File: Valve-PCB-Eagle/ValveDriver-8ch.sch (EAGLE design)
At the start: 17 parts, among them IC1 ULQ2803A, J10 Valve 3, J11 Valve 2, J12 Valve 1, J4 POWER_JACK, J5 Valve 8, J6 Valve 7, J7 Valve 6, J8 Valve 5, J9 Valve 4

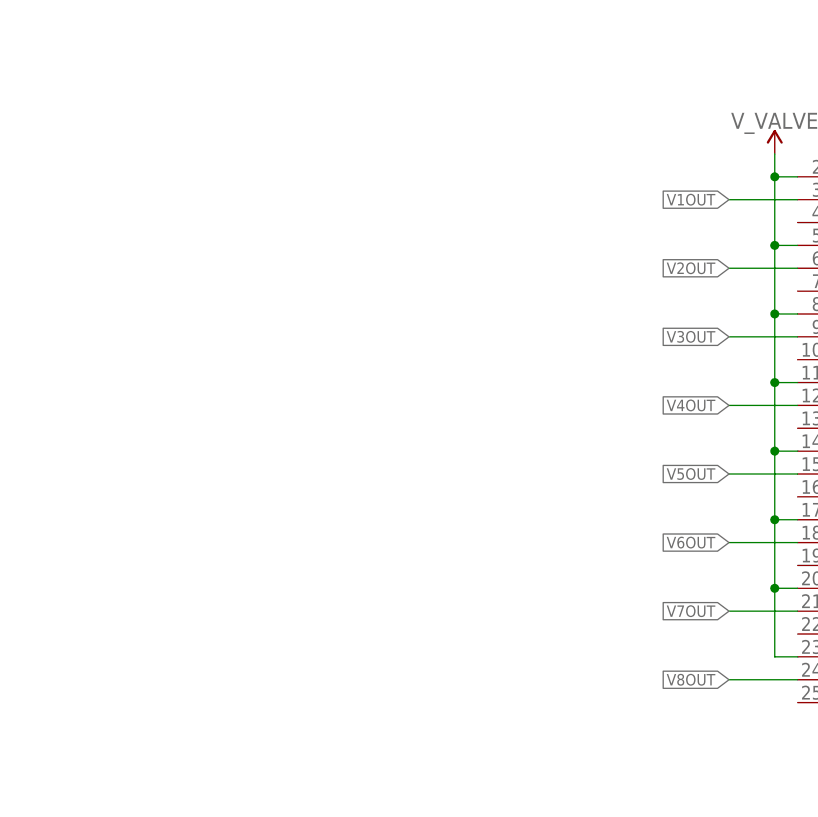
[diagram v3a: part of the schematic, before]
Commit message: [Valve] Add momentary push buttons (fixes #1)
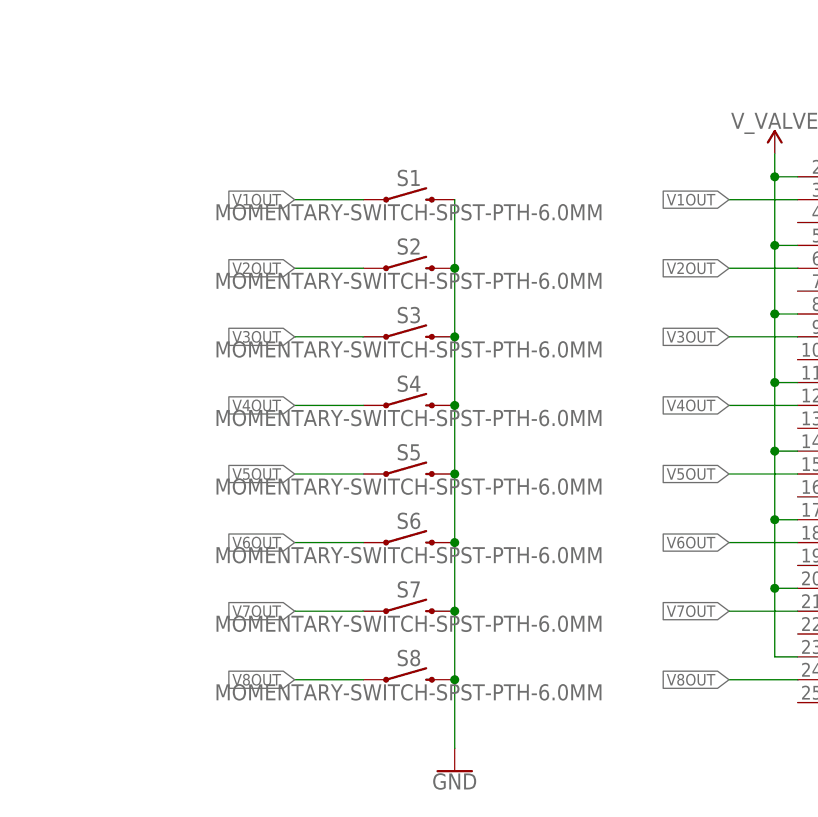
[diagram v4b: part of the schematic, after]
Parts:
- added S1, S2, S3, S4, S5, S6, S7, S8: MOMENTARY-SWITCH-SPST-PTH-6.0MM, SparkFun-Switches:MOMENTARY-SWITCH-SPST-PTH-6.0MM
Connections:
- net GND: now also S1.2, S2.2, S3.2, S4.2, S5.2, S6.2, S7.2, S8.2
- net V1OUT: now also S1.1
- net V2OUT: now also S2.1
- net V3OUT: now also S3.1
- net V4OUT: now also S4.1
- net V5OUT: now also S5.1
- net V6OUT: now also S6.1
- net V7OUT: now also S7.1
- net V8OUT: now also S8.1
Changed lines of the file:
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@@
 <part name="J2" library="SparkFun-Connectors" library_urn="urn:adsk.eagle:library:513" deviceset="CONN_24" device="" package3d_urn="urn:adsk.eagle:package:38202/1"/>
 <part name="SUPPLY13" library="SparkFun-PowerSymbols" library_urn="urn:adsk.eagle:library:530" deviceset="VCC_1" device="" value="V_VALVE"/>
+<part name="S1" library="SparkFun-Switches" library_urn="urn:adsk.eagle:library:535" deviceset="MOMENTARY-SWITCH-SPST" device="-PTH-6.0MM" package3d_urn="urn:adsk.eagle:package:40163/1"/>
+<part name="S2" library="SparkFun-Switches" library_urn="urn:adsk.eagle:library:535" deviceset="MOMENTARY-SWITCH-SPST" device="-PTH-6.0MM" package3d_urn="urn:adsk.eagle:package:40163/1"/>
+<part name="S3" library="SparkFun-Switches" library_urn="urn:adsk.eagle:library:535" deviceset="MOMENTARY-SWITCH-SPST" device="-PTH-6.0MM" package3d_urn="urn:adsk.eagle:package:40163/1"/>
+<part name="S4" library="SparkFun-Switches" library_urn="urn:adsk.eagle:library:535" deviceset="MOMENTARY-SWITCH-SPST" device="-PTH-6.0MM" package3d_urn="urn:adsk.eagle:package:40163/1"/>
+<part name="S5" library="SparkFun-Switches" library_urn="urn:adsk.eagle:library:535" deviceset="MOMENTARY-SWITCH-SPST" device="-PTH-6.0MM" package3d_urn="urn:adsk.eagle:package:40163/1"/>
+<part name="S6" library="SparkFun-Switches" library_urn="urn:adsk.eagle:library:535" deviceset="MOMENTARY-SWITCH-SPST" device="-PTH-6.0MM" package3d_urn="urn:adsk.eagle:package:40163/1"/>
+<part name="S7" library="SparkFun-Switches" library_urn="urn:adsk.eagle:library:535" deviceset="MOMENTARY-SWITCH-SPST" device="-PTH-6.0MM" package3d_urn="urn:adsk.eagle:package:40163/1"/>
+<part name="S8" library="SparkFun-Switches" library_urn="urn:adsk.eagle:library:535" deviceset="MOMENTARY-SWITCH-SPST" device="-PTH-6.0MM" package3d_urn="urn:adsk.eagle:package:40163/1"/>
+<part name="GND1" library="SparkFun-PowerSymbols" deviceset="GND" device=""/>
 </parts>
 <sheets>
@@
 <attribute name="VALUE" x="76.2" y="7.874" size="1.778" layer="96" align="bottom-center"/>
 </instance>
+<instance part="S1" gate="G$1" x="35.56" y="0" smashed="yes">
+<attribute name="NAME" x="35.56" y="1.524" size="1.778" layer="95" font="vector" align="bottom-center"/>
+<attribute name="VALUE" x="35.56" y="-0.508" size="1.778" layer="96" font="vector" align="top-center"/>
+</instance>
+<instance part="S2" gate="G$1" x="35.56" y="-7.62" smashed="yes">
+<attribute name="NAME" x="35.56" y="-6.096" size="1.778" layer="95" font="vector" align="bottom-center"/>
+<attribute name="VALUE" x="35.56" y="-8.128" size="1.778" layer="96" font="vector" align="top-center"/>
+</instance>
+<instance part="S3" gate="G$1" x="35.56" y="-15.24" smashed="yes">
+<attribute name="NAME" x="35.56" y="-13.716" size="1.778" layer="95" font="vector" align="bottom-center"/>
+<attribute name="VALUE" x="35.56" y="-15.748" size="1.778" layer="96" font="vector" align="top-center"/>
+</instance>
+<instance part="S4" gate="G$1" x="35.56" y="-22.86" smashed="yes">
+<attribute name="NAME" x="35.56" y="-21.336" size="1.778" layer="95" font="vector" align="bottom-center"/>
+<attribute name="VALUE" x="35.56" y="-23.368" size="1.778" layer="96" font="vector" align="top-center"/>
+</instance>
+<instance part="S5" gate="G$1" x="35.56" y="-30.48" smashed="yes">
+<attribute name="NAME" x="35.56" y="-28.956" size="1.778" layer="95" font="vector" align="bottom-center"/>
+<attribute name="VALUE" x="35.56" y="-30.988" size="1.778" layer="96" font="vector" align="top-center"/>
+</instance>
+<instance part="S6" gate="G$1" x="35.56" y="-38.1" smashed="yes">
+<attribute name="NAME" x="35.56" y="-36.576" size="1.778" layer="95" font="vector" align="bottom-center"/>
+<attribute name="VALUE" x="35.56" y="-38.608" size="1.778" layer="96" font="vector" align="top-center"/>
+</instance>
+<instance part="S7" gate="G$1" x="35.56" y="-45.72" smashed="yes">
+<attribute name="NAME" x="35.56" y="-44.196" size="1.778" layer="95" font="vector" align="bottom-center"/>
+<attribute name="VALUE" x="35.56" y="-46.228" size="1.778" layer="96" font="vector" align="top-center"/>
+</instance>
+<instance part="S8" gate="G$1" x="35.56" y="-53.34" smashed="yes">
+<attribute name="NAME" x="35.56" y="-51.816" size="1.778" layer="95" font="vector" align="bottom-center"/>
+<attribute name="VALUE" x="35.56" y="-53.848" size="1.778" layer="96" font="vector" align="top-center"/>
+</instance>
+<instance part="GND1" gate="1" x="40.64" y="-63.5" smashed="yes">
+<attribute name="VALUE" x="40.64" y="-63.754" size="1.778" layer="96" align="top-center"/>
+</instance>
 </instances>
 <busses>
@@
 <pinref part="J14" gate="G$1" pin="1"/>
 <pinref part="GND11" gate="1" pin="GND"/>
+</segment>
+<segment>
+<pinref part="GND1" gate="1" pin="GND"/>
+<pinref part="S8" gate="G$1" pin="2"/>
+<wire x1="40.64" y1="-60.96" x2="40.64" y2="-53.34" width="0.1524" layer="91"/>
+<pinref part="S7" gate="G$1" pin="2"/>
+<wire x1="40.64" y1="-53.34" x2="40.64" y2="-45.72" width="0.1524" layer="91"/>
+<junction x="40.64" y="-53.34"/>
+<pinref part="S6" gate="G$1" pin="2"/>
+<wire x1="40.64" y1="-45.72" x2="40.64" y2="-38.1" width="0.1524" layer="91"/>
+<junction x="40.64" y="-45.72"/>
+<pinref part="S5" gate="G$1" pin="2"/>
+<wire x1="40.64" y1="-38.1" x2="40.64" y2="-30.48" width="0.1524" layer="91"/>
+<junction x="40.64" y="-38.1"/>
+<pinref part="S4" gate="G$1" pin="2"/>
+<wire x1="40.64" y1="-30.48" x2="40.64" y2="-22.86" width="0.1524" layer="91"/>
+<junction x="40.64" y="-30.48"/>
+<pinref part="S3" gate="G$1" pin="2"/>
+<wire x1="40.64" y1="-22.86" x2="40.64" y2="-15.24" width="0.1524" layer="91"/>
+<junction x="40.64" y="-22.86"/>
+<pinref part="S2" gate="G$1" pin="2"/>
+<wire x1="40.64" y1="-15.24" x2="40.64" y2="-7.62" width="0.1524" layer="91"/>
+<junction x="40.64" y="-15.24"/>
+<pinref part="S1" gate="G$1" pin="2"/>
+<wire x1="40.64" y1="-7.62" x2="40.64" y2="0" width="0.1524" layer="91"/>
+<junction x="40.64" y="-7.62"/>
 </segment>
 </net>
@@
 <label x="71.12" y="-53.34" size="1.27" layer="95" rot="R180" xref="yes"/>
 </segment>
+<segment>
+<wire x1="30.48" y1="-53.34" x2="22.86" y2="-53.34" width="0.1524" layer="91"/>
+<label x="22.86" y="-53.34" size="1.27" layer="95" rot="R180" xref="yes"/>
+<pinref part="S8" gate="G$1" pin="1"/>
+</segment>
 </net>
 <net name="V7OUT" class="1">
@@
 <label x="71.12" y="-45.72" size="1.27" layer="95" rot="R180" xref="yes"/>
 </segment>
+<segment>
+<wire x1="30.48" y1="-45.72" x2="22.86" y2="-45.72" width="0.1524" layer="91"/>
+<label x="22.86" y="-45.72" size="1.27" layer="95" rot="R180" xref="yes"/>
+<pinref part="S7" gate="G$1" pin="1"/>
+</segment>
 </net>
 <net name="V6OUT" class="1">
@@
 <label x="71.12" y="-38.1" size="1.27" layer="95" rot="R180" xref="yes"/>
 </segment>
+<segment>
+<wire x1="30.48" y1="-38.1" x2="22.86" y2="-38.1" width="0.1524" layer="91"/>
+<label x="22.86" y="-38.1" size="1.27" layer="95" rot="R180" xref="yes"/>
+<pinref part="S6" gate="G$1" pin="1"/>
+</segment>
 </net>
 <net name="V5OUT" class="1">
@@
 <label x="71.12" y="-30.48" size="1.27" layer="95" rot="R180" xref="yes"/>
 </segment>
+<segment>
+<wire x1="30.48" y1="-30.48" x2="22.86" y2="-30.48" width="0.1524" layer="91"/>
+<label x="22.86" y="-30.48" size="1.27" layer="95" rot="R180" xref="yes"/>
+<pinref part="S5" gate="G$1" pin="1"/>
+</segment>
 </net>
 <net name="V4OUT" class="1">
@@
 <label x="71.12" y="-22.86" size="1.27" layer="95" rot="R180" xref="yes"/>
 </segment>
+<segment>
+<wire x1="30.48" y1="-22.86" x2="22.86" y2="-22.86" width="0.1524" layer="91"/>
+<label x="22.86" y="-22.86" size="1.27" layer="95" rot="R180" xref="yes"/>
+<pinref part="S4" gate="G$1" pin="1"/>
+</segment>
 </net>
 <net name="V3OUT" class="1">
@@
 <label x="71.12" y="-15.24" size="1.27" layer="95" rot="R180" xref="yes"/>
 </segment>
+<segment>
+<wire x1="30.48" y1="-15.24" x2="22.86" y2="-15.24" width="0.1524" layer="91"/>
+<label x="22.86" y="-15.24" size="1.27" layer="95" rot="R180" xref="yes"/>
+<pinref part="S3" gate="G$1" pin="1"/>
+</segment>
 </net>
 <net name="V2OUT" class="1">
@@
 <label x="71.12" y="-7.62" size="1.27" layer="95" rot="R180" xref="yes"/>
 </segment>
+<segment>
+<wire x1="30.48" y1="-7.62" x2="22.86" y2="-7.62" width="0.1524" layer="91"/>
+<label x="22.86" y="-7.62" size="1.27" layer="95" rot="R180" xref="yes"/>
+<pinref part="S2" gate="G$1" pin="1"/>
+</segment>
 </net>
 <net name="V1OUT" class="1">
@@
 <label x="71.12" y="0" size="1.27" layer="95" rot="R180" xref="yes"/>
 </segment>
-</net>
+<segment>
+<wire x1="30.48" y1="0" x2="22.86" y2="0" width="0.1524" layer="91"/>
+<label x="22.86" y="0" size="1.27" layer="95" rot="R180" xref="yes"/>
+<pinref part="S1" gate="G$1" pin="1"/>
+</segment>
+</net>

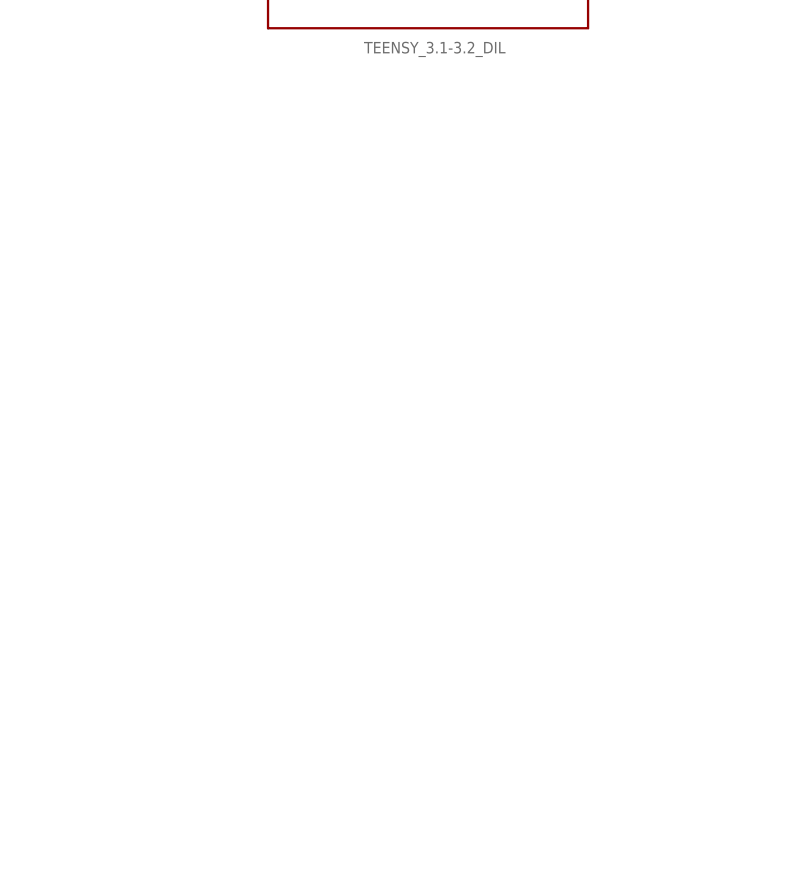
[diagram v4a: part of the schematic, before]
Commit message: [Valve] Silkscreen improvements
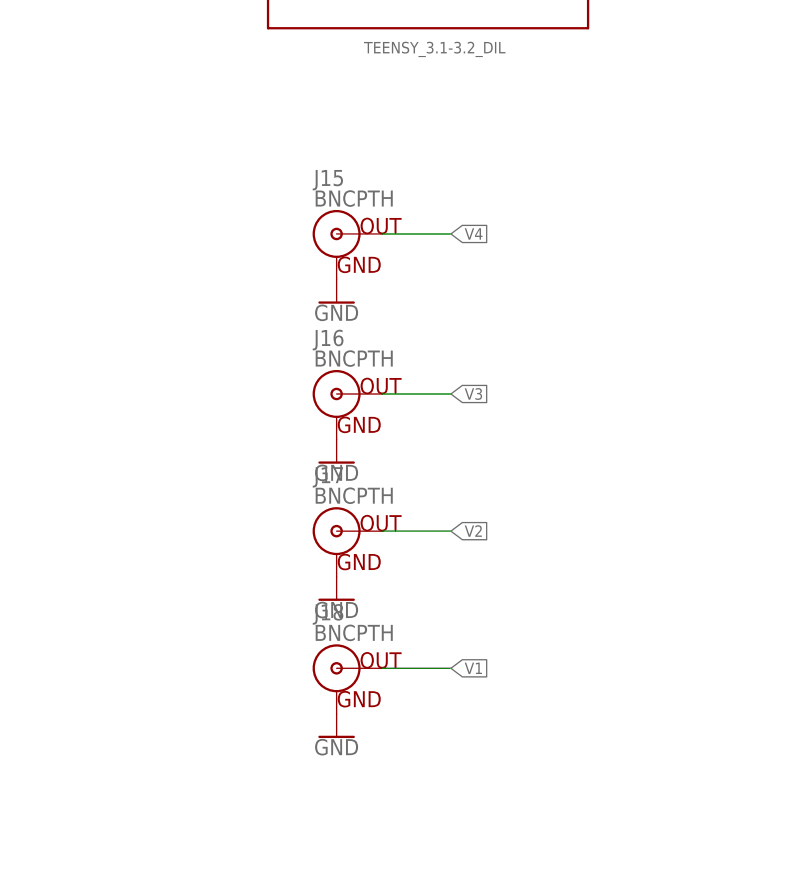
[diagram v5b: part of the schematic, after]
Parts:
- added J15, J16, J17, J18: BNCPTH, SparkFun-Connectors:BNCPTH
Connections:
- net GND: now also J15.GND, J16.GND, J17.GND, J18.GND
- net V1: now also J18.OUT
- net V2: now also J17.OUT
- net V3: now also J16.OUT
- net V4: now also J15.OUT
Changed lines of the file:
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@@
 <part name="S8" library="SparkFun-Switches" library_urn="urn:adsk.eagle:library:535" deviceset="MOMENTARY-SWITCH-SPST" device="-PTH-6.0MM" package3d_urn="urn:adsk.eagle:package:40163/1"/>
 <part name="GND1" library="SparkFun-PowerSymbols" deviceset="GND" device=""/>
+<part name="J15" library="SparkFun-Connectors" library_urn="urn:adsk.eagle:library:513" deviceset="BNC" device="PTH" package3d_urn="urn:adsk.eagle:package:38019/1"/>
+<part name="J16" library="SparkFun-Connectors" library_urn="urn:adsk.eagle:library:513" deviceset="BNC" device="PTH" package3d_urn="urn:adsk.eagle:package:38019/1"/>
+<part name="J17" library="SparkFun-Connectors" library_urn="urn:adsk.eagle:library:513" deviceset="BNC" device="PTH" package3d_urn="urn:adsk.eagle:package:38019/1"/>
+<part name="J18" library="SparkFun-Connectors" library_urn="urn:adsk.eagle:library:513" deviceset="BNC" device="PTH" package3d_urn="urn:adsk.eagle:package:38019/1"/>
+<part name="GND5" library="SparkFun-PowerSymbols" deviceset="GND" device=""/>
+<part name="GND6" library="SparkFun-PowerSymbols" deviceset="GND" device=""/>
+<part name="GND12" library="SparkFun-PowerSymbols" deviceset="GND" device=""/>
+<part name="GND13" library="SparkFun-PowerSymbols" deviceset="GND" device=""/>
 </parts>
 <sheets>
@@
 <instance part="GND1" gate="1" x="40.64" y="-63.5" smashed="yes">
 <attribute name="VALUE" x="40.64" y="-63.754" size="1.778" layer="96" align="top-center"/>
+</instance>
+<instance part="J15" gate="G$1" x="-50.8" y="2.54" smashed="yes">
+<attribute name="NAME" x="-53.34" y="7.874" size="1.778" layer="95" font="vector"/>
+<attribute name="VALUE" x="-53.34" y="5.588" size="1.778" layer="96" font="vector"/>
+</instance>
+<instance part="J16" gate="G$1" x="-50.8" y="-15.24" smashed="yes">
+<attribute name="NAME" x="-53.34" y="-9.906" size="1.778" layer="95" font="vector"/>
+<attribute name="VALUE" x="-53.34" y="-12.192" size="1.778" layer="96" font="vector"/>
+</instance>
+<instance part="J17" gate="G$1" x="-50.8" y="-30.48" smashed="yes">
+<attribute name="NAME" x="-53.34" y="-25.146" size="1.778" layer="95" font="vector"/>
+<attribute name="VALUE" x="-53.34" y="-27.432" size="1.778" layer="96" font="vector"/>
+</instance>
+<instance part="J18" gate="G$1" x="-50.8" y="-45.72" smashed="yes">
+<attribute name="NAME" x="-53.34" y="-40.386" size="1.778" layer="95" font="vector"/>
+<attribute name="VALUE" x="-53.34" y="-42.672" size="1.778" layer="96" font="vector"/>
+</instance>
+<instance part="GND5" gate="1" x="-50.8" y="-5.08" smashed="yes">
+<attribute name="VALUE" x="-50.8" y="-5.334" size="1.778" layer="96" align="top-center"/>
+</instance>
+<instance part="GND6" gate="1" x="-50.8" y="-22.86" smashed="yes">
+<attribute name="VALUE" x="-50.8" y="-23.114" size="1.778" layer="96" align="top-center"/>
+</instance>
+<instance part="GND12" gate="1" x="-50.8" y="-38.1" smashed="yes">
+<attribute name="VALUE" x="-50.8" y="-38.354" size="1.778" layer="96" align="top-center"/>
+</instance>
+<instance part="GND13" gate="1" x="-50.8" y="-53.34" smashed="yes">
+<attribute name="VALUE" x="-50.8" y="-53.594" size="1.778" layer="96" align="top-center"/>
 </instance>
 </instances>
@@
 <wire x1="40.64" y1="-7.62" x2="40.64" y2="0" width="0.1524" layer="91"/>
 <junction x="40.64" y="-7.62"/>
+</segment>
+<segment>
+<pinref part="J15" gate="G$1" pin="GND"/>
+<pinref part="GND5" gate="1" pin="GND"/>
+</segment>
+<segment>
+<pinref part="J16" gate="G$1" pin="GND"/>
+<pinref part="GND6" gate="1" pin="GND"/>
+</segment>
+<segment>
+<pinref part="J17" gate="G$1" pin="GND"/>
+<pinref part="GND12" gate="1" pin="GND"/>
+</segment>
+<segment>
+<pinref part="J18" gate="G$1" pin="GND"/>
+<pinref part="GND13" gate="1" pin="GND"/>
 </segment>
 </net>
@@
 <label x="20.32" y="55.88" size="1.778" layer="95"/>
 </segment>
+<segment>
+<pinref part="J18" gate="G$1" pin="OUT"/>
+<wire x1="-45.72" y1="-45.72" x2="-38.1" y2="-45.72" width="0.1524" layer="91"/>
+<label x="-38.1" y="-45.72" size="1.27" layer="95" xref="yes"/>
+</segment>
 </net>
 <net name="V2" class="0">
@@
 <label x="20.32" y="58.42" size="1.778" layer="95"/>
 </segment>
+<segment>
+<pinref part="J17" gate="G$1" pin="OUT"/>
+<wire x1="-45.72" y1="-30.48" x2="-38.1" y2="-30.48" width="0.1524" layer="91"/>
+<label x="-38.1" y="-30.48" size="1.27" layer="95" xref="yes"/>
+</segment>
 </net>
 <net name="V4" class="0">
@@
 <label x="20.32" y="63.5" size="1.778" layer="95"/>
 </segment>
+<segment>
+<pinref part="J15" gate="G$1" pin="OUT"/>
+<wire x1="-45.72" y1="2.54" x2="-38.1" y2="2.54" width="0.1524" layer="91"/>
+<label x="-38.1" y="2.54" size="1.27" layer="95" xref="yes"/>
+</segment>
 </net>
 <net name="V3" class="0">
@@
 <label x="20.32" y="60.96" size="1.778" layer="95"/>
 </segment>
+<segment>
+<pinref part="J16" gate="G$1" pin="OUT"/>
+<wire x1="-45.72" y1="-15.24" x2="-38.1" y2="-15.24" width="0.1524" layer="91"/>
+<label x="-38.1" y="-15.24" size="1.27" layer="95" xref="yes"/>
+</segment>
 </net>
 <net name="V5" class="0">
@@
 </segment>
 </net>
-<net name="3.3V" class="0">
+<net name="3.3V" class="1">
 <segment>
 <pinref part="SUPPLY15" gate="G$1" pin="3.3V"/>
@@
 </segment>
 </net>
-<net name="V_IN_TEENSY" class="0">
+<net name="V_IN_TEENSY" class="1">
 <segment>
 <pinref part="U$1" gate="G$1" pin="VIN"/>
